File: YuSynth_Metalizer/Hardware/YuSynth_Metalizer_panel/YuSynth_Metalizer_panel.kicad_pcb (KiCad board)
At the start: 2 copper layers, 30 x 128.5 mm, 0 parts

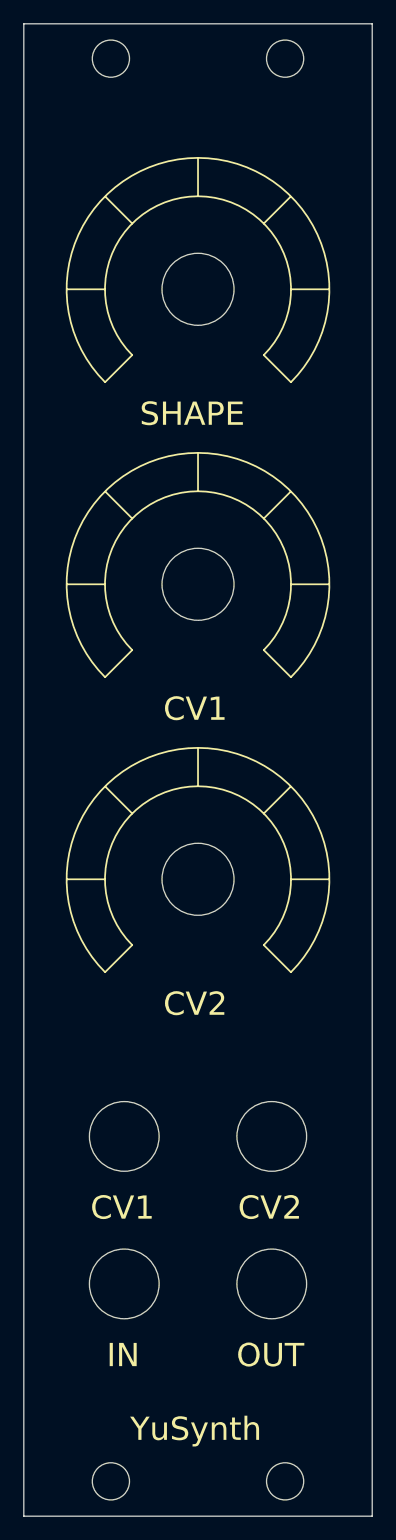
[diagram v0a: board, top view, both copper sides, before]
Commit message: Finished panel & redid file structure
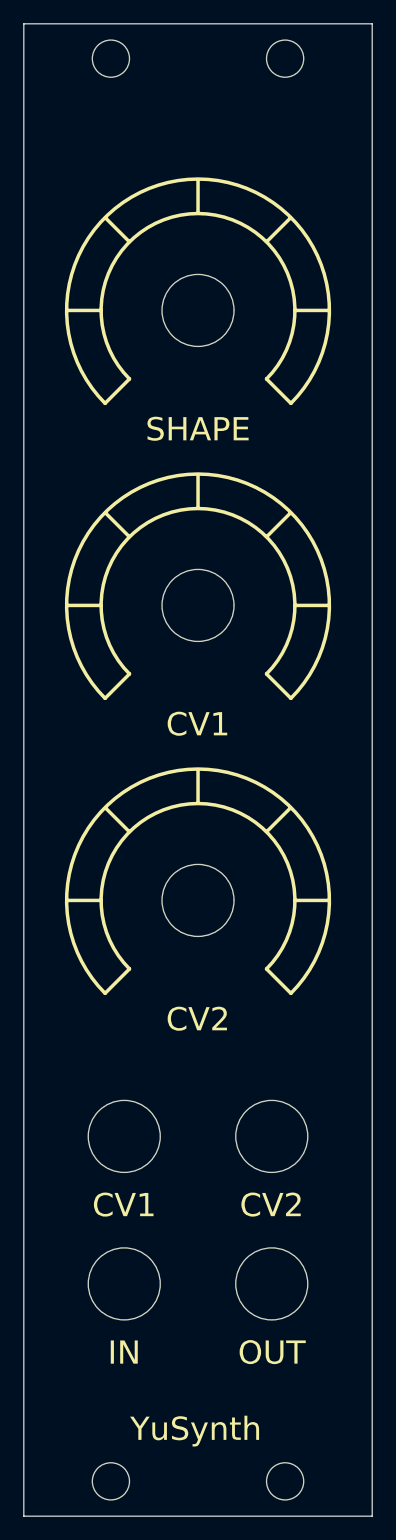
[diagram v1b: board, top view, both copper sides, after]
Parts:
- added REF**: 3.5mm_thonkiconn, 1_Jacks:3.5mm_thonkiconn, F.Cu at (6.35, 95.8)
- added REF**: 3.5mm_thonkiconn, 1_Jacks:3.5mm_thonkiconn, F.Cu at (-6.35, 95.8)
- added REF**: 16mm_Knob, 1_Knob_Scales:16mm_Knob, F.Cu at (0.00, 75.5)
- added REF**: 16mm_Knob, 1_Knob_Scales:16mm_Knob, F.Cu at (0.00, 50.1)
- added REF**: 3.5mm_thonkiconn, 1_Jacks:3.5mm_thonkiconn, F.Cu at (-6.35, 108.5)
- added REF**: 3.5mm_thonkiconn, 1_Jacks:3.5mm_thonkiconn, F.Cu at (6.35, 108.5)
- added REF**: 16mm_Knob, 1_Knob_Scales:16mm_Knob, F.Cu at (0.00, 24.7)
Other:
- outline, holes or cut-outs redrawn
- board text removed: "CV1"
- board text removed: "CV2"
- board text removed: "IN"
- board text removed: "OUT"
- board text removed: "SHAPE"

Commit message: Redid all boards
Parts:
- moved REF** 2.50 mm to (-6.35, 111.0)
- moved REF** 2.50 mm to (6.35, 111.0)
- moved REF** 0.26 mm to (6.35, 96.1)
- moved REF** 0.26 mm to (-6.35, 96.1)
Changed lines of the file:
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@@
   (net 0 "")
   (footprint "1_Jacks:3.5mm_thonkiconn" (layer "F.Cu")
-    (at 6.35 95.8)
+    (at 6.35 96.064)
     (fp_text reference "REF**" (at 0 -0.5 unlocked) (layer "F.SilkS") hide
         (effects (font (size 1 1) (thickness 0.1)))
@@
   )
   (footprint "1_Jacks:3.5mm_thonkiconn" (layer "F.Cu")
-    (at -6.35 95.8)
+    (at -6.35 96.064)
     (fp_text reference "REF**" (at 0 -0.5 unlocked) (layer "F.SilkS") hide
         (effects (font (size 1 1) (thickness 0.1)))
@@
   )
   (footprint "1_Jacks:3.5mm_thonkiconn" (layer "F.Cu")
-    (at -6.35 108.5)
+    (at -6.35 110.998)
     (fp_text reference "REF**" (at 0 -0.5 unlocked) (layer "F.SilkS") hide
         (effects (font (size 1 1) (thickness 0.1)))
@@
   )
   (footprint "1_Jacks:3.5mm_thonkiconn" (layer "F.Cu")
-    (at 6.35 108.5)
+    (at 6.35 110.998)
     (fp_text reference "REF**" (at 0 -0.5 unlocked) (layer "F.SilkS") hide
         (effects (font (size 1 1) (thickness 0.1)))
